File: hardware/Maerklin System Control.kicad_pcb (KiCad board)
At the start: 2 copper layers, 83 x 55 mm, 39 parts, among them J1 Female Header, J2 Output, J3 Input, J4 Conn_S3 Mini, SW1 UP, SW2 RIGHT, SW3 DOWN, SW4 LEFT, SW5 SELECT, SW6 BACK

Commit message: add sponsoring
Signed-off-by: Peter Siegmund <developer@mars3142.org>
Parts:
- added G***: LOGO, sponsors:PCBWay (5mm), B.Cu at (130.2, 51.0)
- added REF**: KiCad-Logo_5mm_SilkScreen, Symbol:KiCad-Logo_5mm_SilkScreen, B.Cu at (130.3, 46.3)

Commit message: switch from global net labels to local
Signed-off-by: Peter Siegmund <developer@mars3142.org>
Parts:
- removed the REF** at (130.3, 46.3)
- removed kibuzzard-67898040: G***, kibuzzard-67898040
- removed kibuzzard-67898062: G***, kibuzzard-67898062
- removed kibuzzard-67898074: G***, kibuzzard-67898074
- removed kibuzzard-67898084: G***, kibuzzard-67898084
- added REF**: KiCad-Logo_6mm_SilkScreen, Symbol:KiCad-Logo_6mm_SilkScreen, B.Cu at (130.1, 45.4)
- added kibuzzard-68D2E6D4: G***, kibuzzard-68D2E6D4, B.Cu at (73.2, 48.7)
- added kibuzzard-68D2E6E4: G***, kibuzzard-68D2E6E4, B.Cu at (73.2, 51.3)
- added kibuzzard-68D2E6EB: G***, kibuzzard-68D2E6EB, B.Cu at (73.2, 53.8)
- added kibuzzard-68D2E6F2: G***, kibuzzard-68D2E6F2, B.Cu at (73.2, 56.4)
- J1: footprint Connector_PinSocket_2.54mm:PinSocket_1x04_P2.54mm_Vertical -> Connector_PinSocket_2.54mm:PinSocket_1x04_P2.54mm_Horizontal
- moved J1 7.15 mm to (76.5, 48.8), turned to 180 degrees
- moved kibuzzard-6859B258 6.06 mm to (78.5, 45.9), turned to 180 degrees
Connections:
- net BACK renamed /BACK
- net DOUT renamed /DOUT
- net DOWN renamed /DOWN
- net LED renamed /LED
- net LEFT renamed /LEFT
- net RIGHT renamed /RIGHT
- net SCK renamed /SCK
- net SDA renamed /SDA
- net SELECT renamed /SELECT
- net UP renamed /UP
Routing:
- net +5V: track 211.4 -> 225.3 mm, vias 2 -> 0
- net /SDA: track 54.5 -> 41.2 mm
- net /SCK: track 49.6 -> 41.2 mm
- net /SELECT: track 25.8 -> 26.7 mm

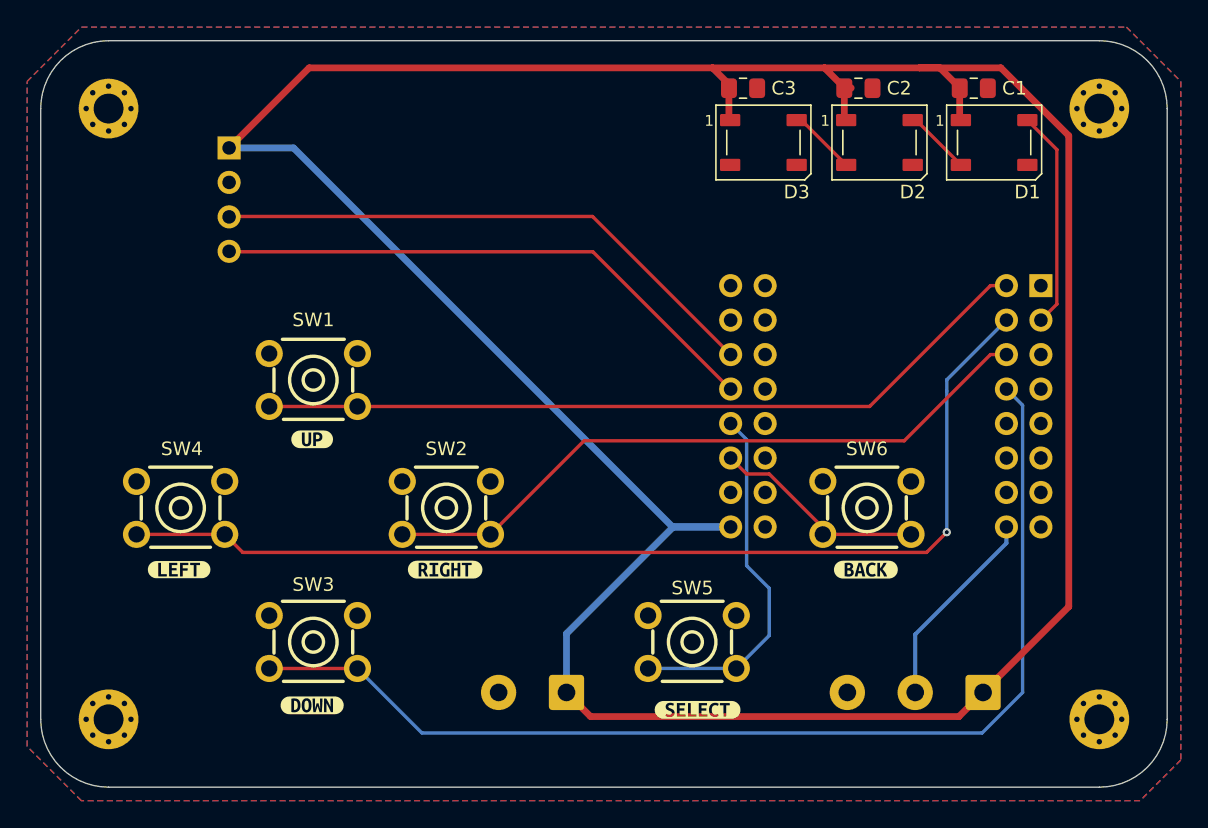
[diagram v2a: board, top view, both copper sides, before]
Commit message: ESP32 C6 support
Signed-off-by: Peter Siegmund <developer@mars3142.org>
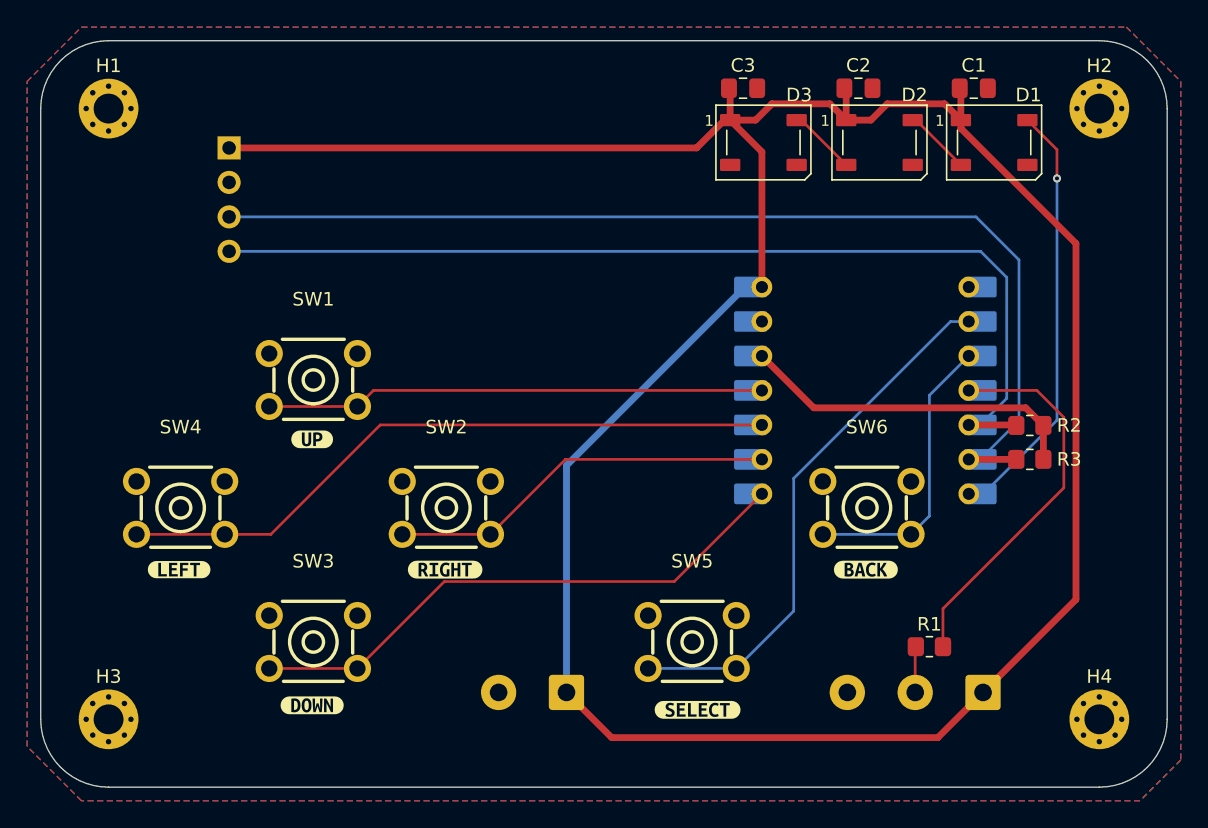
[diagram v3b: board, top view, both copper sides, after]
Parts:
- removed J4: Conn_S3 Mini, wemos:PinSocket_S3 Mini
- removed kibuzzard-67897FC0: G***, kibuzzard-67897FC0
- added R1: 220Ω, Resistor_SMD:R_0805_2012Metric_Pad1.20x1.40mm_HandSolder, F.Cu at (128.1, 85.5)
- added R2: 4,7 kΩ, Resistor_SMD:R_0805_2012Metric_Pad1.20x1.40mm_HandSolder, F.Cu at (135.5, 69.2)
- added R3: 4,7 kΩ, Resistor_SMD:R_0805_2012Metric_Pad1.20x1.40mm_HandSolder, F.Cu at (135.5, 71.7)
- added U1: XIAO-ESP32-C6-DIP, Seeed_Studio_XIAO_Series:XIAO-ESP32-C6-DIP, B.Cu at (123.4, 66.6)
- renumbered J3 to J2, J2 to J3
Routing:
- net /DOWN: track 81.6 -> 41.6 mm
- net /SCK: track 41.2 -> 78.9 mm
- net /SDA: track 41.2 -> 73.3 mm
- net +5V: track 225.3 -> 195.7 mm
- net /LEFT: track 78.3 -> 49.4 mm, vias 1 -> 0
- net Net-(U1-GPIO21_D3): track 0.00 -> 28.4 mm
- net +3V3: track 0.00 -> 25.4 mm
- net /RIGHT: track 50.0 -> 28.8 mm
- net /UP: track 58.0 -> 36.8 mm
- net /LED: track 16.1 -> 31.8 mm, vias 0 -> 1
- net /SELECT: track 26.7 -> 39.9 mm
- net /DOUT: track 15.0 -> 3.39 mm
- net /BACK: track 15.9 -> 21.4 mm
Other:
- board text added: "(c) 2026 by mars3142"
- board text added: "System Control MK3"
- board text removed: "(c) 2025 by mars3142"
- board text removed: "System Control MK2.1"

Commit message: latest KiCad format
Signed-off-by: Peter Siegmund <developer@mars3142.org>
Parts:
- removed J2: Input, TerminalBlock_Phoenix:TerminalBlock_Phoenix_MKDS-1,5-2_1x02_P5.00mm_Horizontal
- removed kibuzzard-678980A4: G***, kibuzzard-678980A4
- removed kibuzzard-678A131B: G***, kibuzzard-678A131B
- removed kibuzzard-678A1332: G***, kibuzzard-678A1332
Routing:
- net +5V: track 195.7 -> 127.0 mm
